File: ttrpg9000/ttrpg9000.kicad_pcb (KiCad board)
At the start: 2 copper layers, 35 parts, among them SW1 SW_SPST, SW2 RotaryEncoder_Switch, SW3 RotaryEncoder_Switch, U1 ATtiny2313A-P, U2 LP2950-3.3_TO92

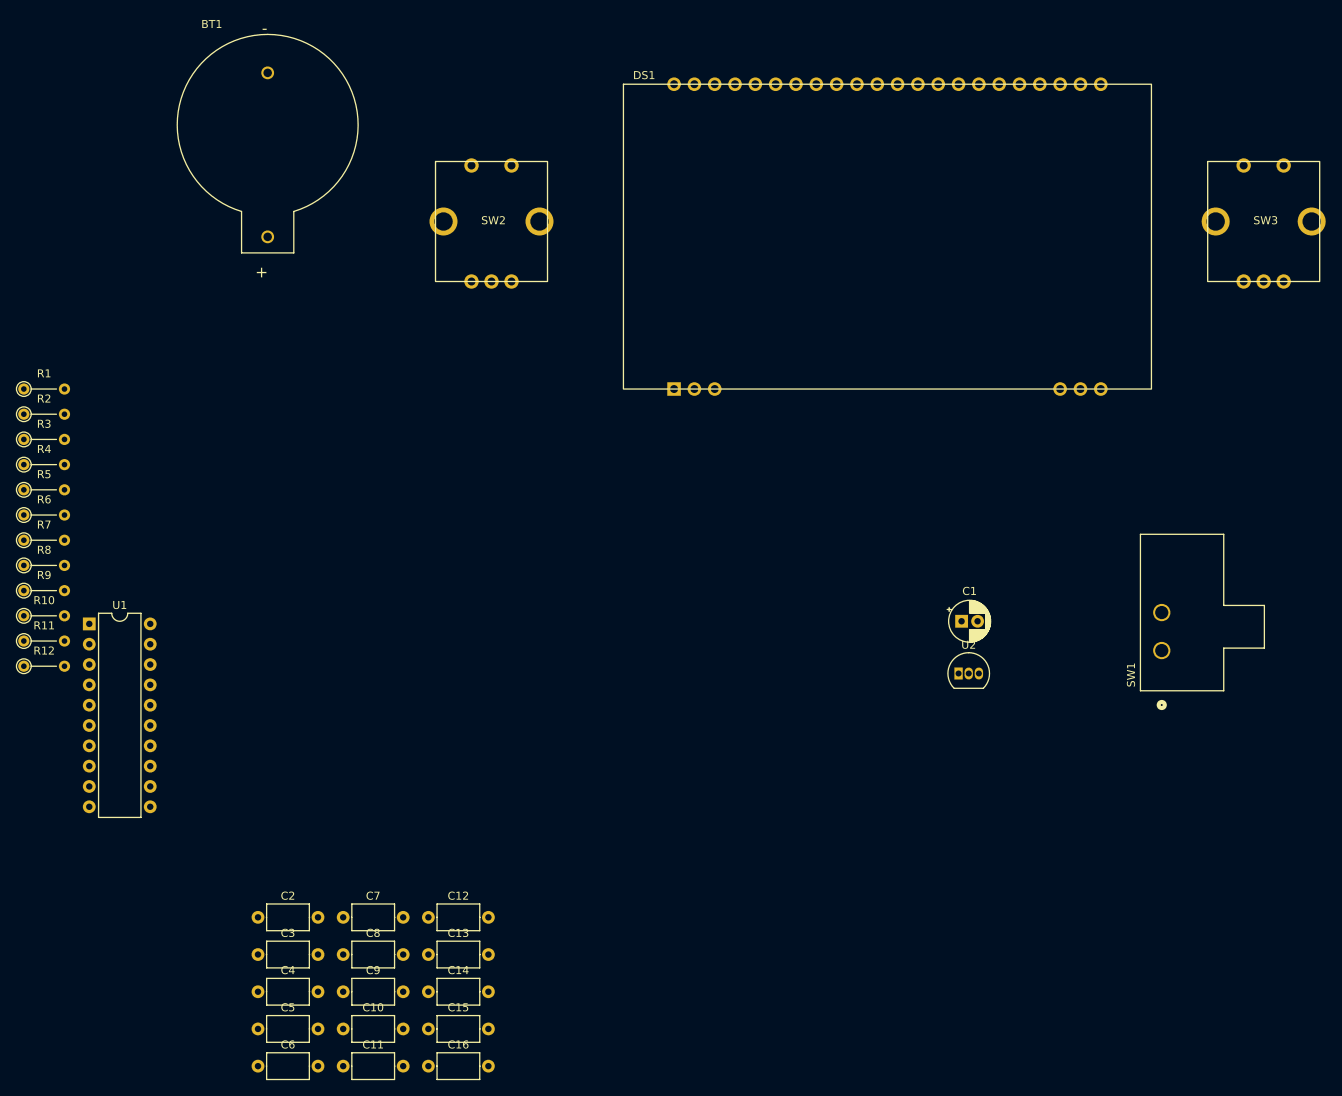
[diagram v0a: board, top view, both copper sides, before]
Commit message: Clean up board layout
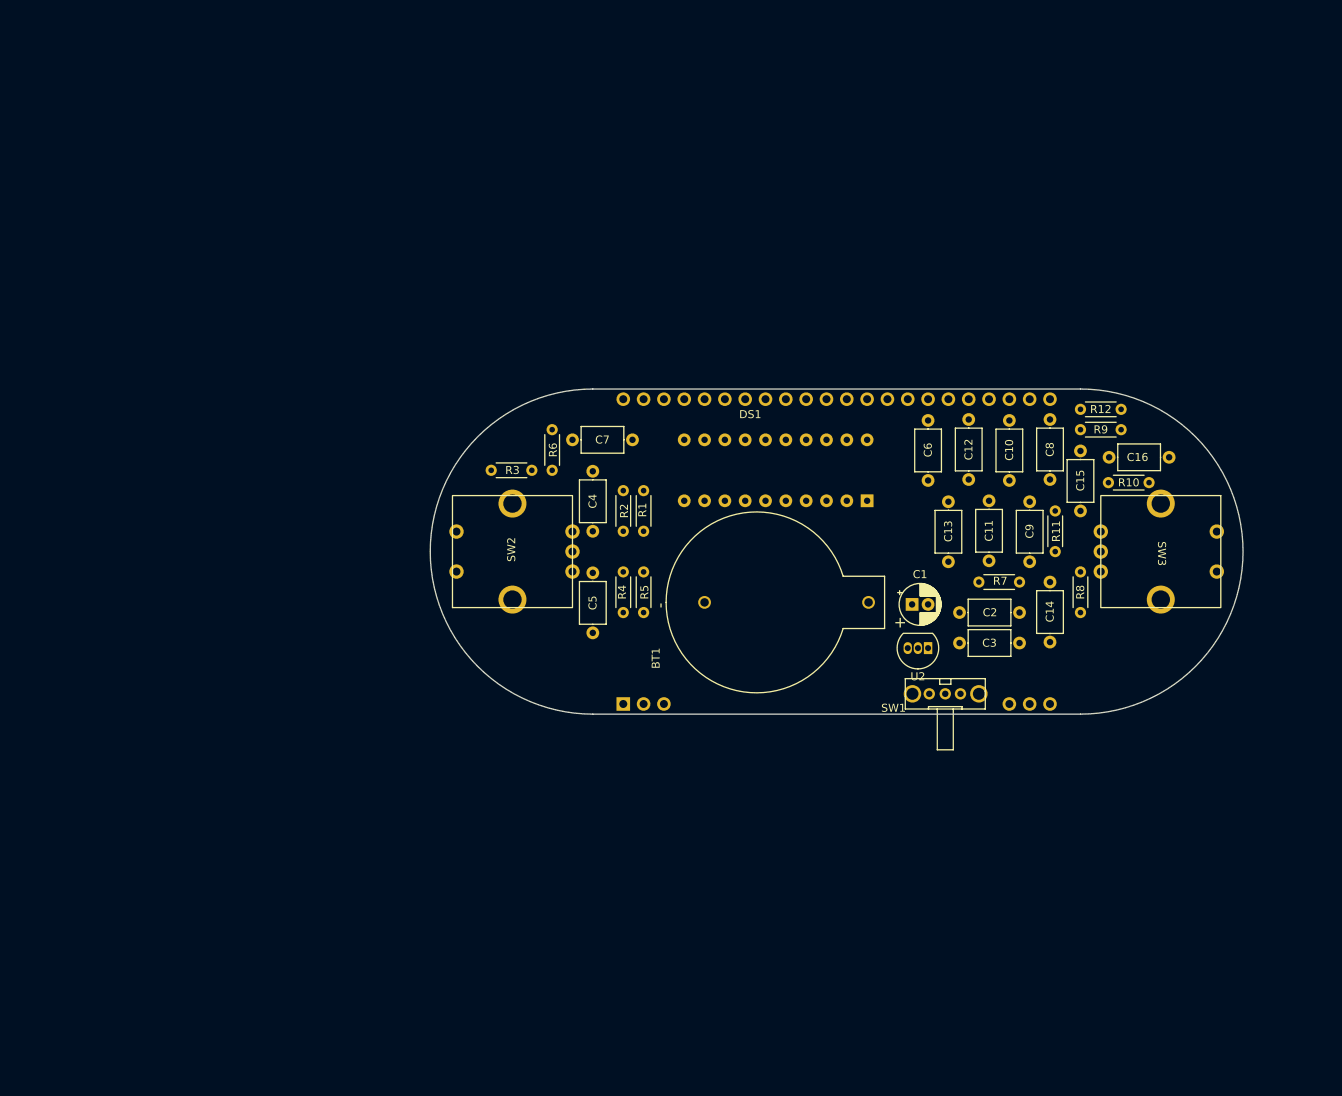
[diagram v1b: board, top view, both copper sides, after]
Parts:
- R1, R10, R11, R12, R2, R3, R4, R5, R6, R7, R8, R9: footprint Resistor_THT:R_Axial_DIN0204_L3.6mm_D1.6mm_P5.08mm_Vertical -> Resistor_THT:R_Axial_DIN0204_L3.6mm_D1.6mm_P5.08mm_Horizontal
- SW1: value SW_SPST -> SW_SPDT; footprint Project:SW3x1_L101011ML04Q_CNK -> Project:OS102011MA1Q
- U1: moved to B.Cu
- moved R10 141.6 mm to (178.8, 85.4), turned to 180 degrees
- moved R9 138.6 mm to (175.3, 78.7), turned to 180 degrees
- moved R12 135.9 mm to (170.2, 76.2)
- moved R8 132.1 mm to (170.2, 96.5), turned to -90 degrees
- moved R11 129.9 mm to (167.0, 88.9), turned to -90 degrees
- moved R7 119.5 mm to (157.5, 97.8)
- moved C6 116.3 mm to (151.1, 77.6), turned to -90 degrees
- moved C16 114.2 mm to (173.8, 82.2)
- moved C10 112.8 mm to (161.3, 77.6), turned to -90 degrees
- moved C8 110.8 mm to (166.4, 77.5), turned to -90 degrees
- moved C15 108.9 mm to (170.2, 81.4), turned to -90 degrees
- moved C11 107.3 mm to (158.8, 87.6), turned to -90 degrees
- moved C9 105.4 mm to (163.8, 87.8), turned to -90 degrees
- moved U1 98.4 mm to (143.5, 87.6), turned to 90 degrees
- moved C3 95.9 mm to (155.1, 105.4)
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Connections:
- DS1 pad 44: (no net) -> Net-(DS1-~{RESET})
- SW1 pad 1: GND -> Net-(BT1--)
- SW1 pad 2: Net-(BT1--) -> GND
- U1 pad 13: Net-(DS1-E) -> Net-(DS1-RS)
- U1 pad 15: Net-(DS1-RS) -> Net-(DS1-E)
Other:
- board outline added: 101.6 x 40.6 mm

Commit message: Finalize v0.1 board layout
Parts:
- added G***: LOGO, Project:GhostWrenchLogo, F.Cu at (134.6, 103.5)
- BT1: moved to B.Cu
- moved SW1 59.3 mm to (105.4, 76.8), turned to 180 degrees
- moved DS1 33.5 mm to (139.7, 92.7)
- moved R9 11.7 mm to (186.0, 83.2)
- moved R3 6.36 mm to (102.8, 83.2)
- moved R6 4.94 mm to (107.9, 80.6), turned to 180 degrees
- moved C7 4.68 mm to (110.6, 82.5)
- moved R12 3.22 mm to (173.3, 76.8)
- moved C4 2.54 mm to (109.2, 94.0)
- moved C16 2.23 mm to (173.3, 80.0)
- moved R10 2.20 mm to (178.4, 83.2)
- moved C1 2.02 mm to (151.1, 101.0), turned to 90 degrees
- moved BT1 1.82 mm to (131.4, 101.0), turned to -90 degrees
- moved SW2 1.43 mm to (106.0, 92.7)
- moved SW3 1.41 mm to (173.3, 92.7)
- moved C15 1.27 mm to (170.2, 80.1)
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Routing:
- net Net-(U1-PD0): track 0.00 -> 47.6 mm
- net Net-(BT1--): track 0.00 -> 31.4 mm
- net Net-(U1-PD1): track 0.00 -> 31.2 mm
- net Net-(U1-PD2): track 0.00 -> 30.9 mm
- net Net-(U1-PD3): track 0.00 -> 25.2 mm
- net Net-(R3-Pad1): track 0.00 -> 17.6 mm
- net +6V: track 0.00 -> 16.1 mm
- net Net-(DS1-V4): track 0.00 -> 14.1 mm
- net Net-(DS1-V0): track 0.00 -> 14.1 mm
- net Net-(DS1-V2): track 0.00 -> 14.0 mm
- net Net-(U1-PD4): track 0.00 -> 13.8 mm
- net Net-(C5-Pad2): track 0.00 -> 13.8 mm
- net Net-(C15-Pad2): track 0.00 -> 13.7 mm
- net Net-(DS1-RS): track 0.00 -> 12.8 mm
- net Net-(DS1-R/~{W}): track 0.00 -> 12.8 mm
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- added copper zone on F.Cu, net +3V3
- added copper zone on B.Cu, net GND
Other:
- board size 101.6 x 40.6 mm -> 104 x 44 mm
- board text added: "TTRPG-9000 v0.1"
